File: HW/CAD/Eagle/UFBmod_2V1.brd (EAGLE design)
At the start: 98.4 x 89.5 mm, 195 parts, among them T0551 MMBT2222, U0501 MIDAS_MCCOG21605B6W-FPTLWI, U0601 MAX5217, U0701 AT86RF215-ZU, U0711 ASVTX-13-D-26.000MHZ-I05-T, U0811 PE4259, U0821 RFX1010, U0881 B39871B3440U410, U0911 FT232HL, U1101 TPS53353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

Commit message: HW - Eagle - V2.1 update to current FPGA implementation
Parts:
- R0971, R0972: value 1kR -> 560R
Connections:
- removed net FPGA_FT_RXD: JB2.83, R0962.2
- removed net FPGA_FT_TXD: JB2.81, R0961.2
- removed net UART0_RXD: JB1.91
- removed net UART0_TXD: JB1.86
- new net FPGA_UART0_RXD: JB1.91, R0961.2
- new net FPGA_UART0_TXD: JB1.86, R0962.2
- net FT_RXLED_D: now also D0971.C; no longer D0971.A
- net FT_TXLED_D: now also D0972.C; no longer D0972.A
- net FT_VCCD: now also D0971.A, D0972.A
- net GND: no longer D0971.C, D0972.C
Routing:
- net FPGA_FT_RXD: track 2.85 -> 0.00 mm
- net FPGA_UART0_TXD: track 0.00 -> 2.84 mm
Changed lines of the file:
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@@
 <attribute name="VALUE" x="68.2625" y="67.6275" size="0.6096" layer="27" font="vector" ratio="10" rot="R270"/>
 </element>
-<element name="R0971" library="df4iah_rcl" package="R0402" value="1kR" x="59.69" y="36.83" smashed="yes" rot="MR270">
+<element name="R0971" library="df4iah_rcl" package="R0402" value="560R" x="59.69" y="36.83" smashed="yes" rot="MR270">
 <attribute name="NAME" x="60.6425" y="35.2425" size="0.6096" layer="26" font="vector" ratio="10" rot="MR90"/>
 <attribute name="VALUE" x="61.2775" y="38.4175" size="0.6096" layer="28" font="vector" ratio="10" rot="MR270"/>
 </element>
-<element name="R0972" library="df4iah_rcl" package="R0402" value="1kR" x="58.42" y="36.83" smashed="yes" rot="MR270">
+<element name="R0972" library="df4iah_rcl" package="R0402" value="560R" x="58.42" y="36.83" smashed="yes" rot="MR270">
 <attribute name="NAME" x="56.8325" y="35.2425" size="0.6096" layer="26" font="vector" ratio="10" rot="MR90"/>
 <attribute name="VALUE" x="60.0075" y="38.4175" size="0.6096" layer="28" font="vector" ratio="10" rot="MR270"/>
@@
 <contactref element="C0921" pad="1"/>
 <contactref element="C0922" pad="1"/>
-<contactref element="D0971" pad="C"/>
-<contactref element="D0972" pad="C"/>
 <contactref element="X1331" pad="1"/>
 <contactref element="X1331" pad="3"/>
@@
 <wire x1="74.93" y1="21.17" x2="77.88" y2="27.96" width="0" layer="19" extent="16-16"/>
 <wire x1="54.61" y1="82.55" x2="54.545" y2="74.945" width="0" layer="19" extent="1-1"/>
-<wire x1="45.72" y1="87.41" x2="49.2125" y2="84.44" width="0" layer="19" extent="1-1"/>
-<wire x1="43.18" y1="87.41" x2="45.72" y2="87.41" width="0" layer="19" extent="1-1"/>
 <wire x1="74.93" y1="12.05" x2="74.93" y2="21.17" width="0" layer="19" extent="16-16"/>
 <wire x1="22.5425" y1="47.3075" x2="33.03" y2="46.21" width="0" layer="19" extent="1-1"/>
@@
 <wire x1="60.0075" y1="48.5425" x2="60.0075" y2="41.91" width="0.1524" layer="16"/>
 <wire x1="60.0075" y1="41.91" x2="60.325" y2="41.5925" width="0.1524" layer="16"/>
+<contactref element="D0971" pad="A"/>
+<contactref element="D0972" pad="A"/>
+<wire x1="43.18" y1="85.31" x2="45.72" y2="85.31" width="0" layer="19" extent="1-1"/>
+<wire x1="59.85" y1="48.7" x2="45.72" y2="85.31" width="0" layer="19" extent="1-16"/>
 </signal>
 <signal name="FT_RESET">
@@
 <wire x1="62.865" y1="47.625" x2="64.12" y2="47.625" width="0.1524" layer="16"/>
 </signal>
-<signal name="FPGA_FT_TXD">
-<contactref element="R0961" pad="2"/>
-<contactref element="JB2" pad="81"/>
-<wire x1="65.42" y1="47.625" x2="63.63" y2="62.81" width="0" layer="19" extent="1-16"/>
-</signal>
 <signal name="FT_RXD">
 <contactref element="U0911" pad="14"/>
@@
 <wire x1="62.5475" y1="45.72" x2="64.77" y2="66.69" width="0" layer="19" extent="1-16"/>
 </signal>
-<signal name="FPGA_FT_RXD">
-<contactref element="R0962" pad="2"/>
-<contactref element="JB2" pad="83"/>
-<wire x1="64.13" y1="62.81" x2="64.135" y2="62.815" width="0.1524" layer="1"/>
-<wire x1="64.135" y1="62.815" x2="64.135" y2="63.8175" width="0.1524" layer="1"/>
-<wire x1="64.135" y1="63.8175" x2="63.5" y2="64.4525" width="0.1524" layer="1"/>
-<wire x1="63.5" y1="64.4525" x2="63.5" y2="65.39" width="0.1524" layer="1"/>
-</signal>
 <signal name="FPGA_FT_RTS">
 <contactref element="R0963" pad="2"/>
@@
 <signal name="FT_TXLED_D">
 <contactref element="R0972" pad="2"/>
-<contactref element="D0972" pad="A"/>
-<wire x1="58.42" y1="36.18" x2="45.72" y2="85.31" width="0" layer="19" extent="1-16"/>
+<contactref element="D0972" pad="C"/>
+<wire x1="58.42" y1="36.18" x2="45.72" y2="87.41" width="0" layer="19" extent="1-16"/>
 </signal>
 <signal name="FT_RXLED_D">
 <contactref element="R0971" pad="2"/>
-<contactref element="D0971" pad="A"/>
-<wire x1="59.69" y1="36.18" x2="43.18" y2="85.31" width="0" layer="19" extent="1-16"/>
+<contactref element="D0971" pad="C"/>
+<wire x1="59.69" y1="36.18" x2="43.18" y2="87.41" width="0" layer="19" extent="1-16"/>
 </signal>
 <signal name="B2W_51">
@@
 <wire x1="4.43" y1="53.34" x2="56.13" y2="59.11" width="0" layer="19" extent="1-1"/>
 </signal>
-<signal name="UART0_TXD">
+<signal name="FPGA_UART0_TXD">
 <contactref element="JB1" pad="86"/>
+<contactref element="R0962" pad="2"/>
+<wire x1="64.135" y1="62.815" x2="64.135" y2="63.8175" width="0.1524" layer="1"/>
+<wire x1="64.135" y1="63.8175" x2="63.5" y2="64.4525" width="0.1524" layer="1"/>
+<wire x1="63.5" y1="64.4525" x2="63.5" y2="65.39" width="0.1524" layer="1"/>
+<wire x1="64.63" y1="27.11" x2="64.135" y2="62.815" width="0" layer="19" extent="1-1"/>
 </signal>
-<signal name="UART0_RXD">
+<signal name="FPGA_UART0_RXD">
 <contactref element="JB1" pad="91"/>
+<contactref element="R0961" pad="2"/>
+<wire x1="66.13" y1="30.81" x2="65.42" y2="47.625" width="0" layer="19" extent="1-16"/>
 </signal>
 </signals>

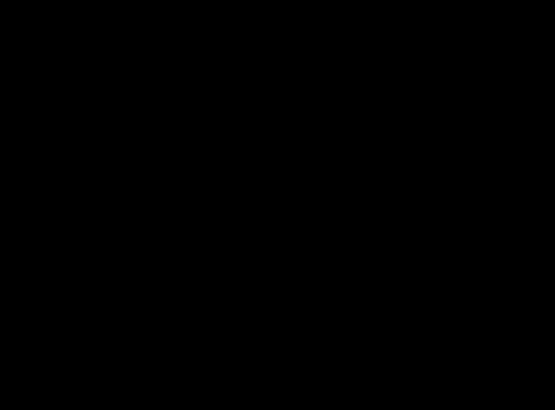
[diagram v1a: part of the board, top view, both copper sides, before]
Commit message: HW - Eagle - V2.1 some signals fixed
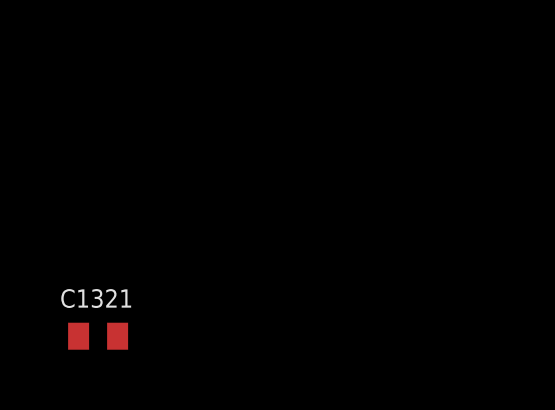
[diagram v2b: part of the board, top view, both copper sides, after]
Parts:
- added C1321: 100nF, df4iah_rcl:C0402
- R1321: value 100R -> 1kR
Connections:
- net FPGA_RESET: now also C1321.2; no longer JB3.41
- net GND: now also C1321.1
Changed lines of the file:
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@@
 </element>
 <element name="S1321" library="df4iah_switch" package="KSR223G_SMD_1POL" value="KSR223G_SMD_1POL" x="36.83" y="73.66" rot="R90"/>
-<element name="R1321" library="df4iah_rcl" package="R0402" value="100R" x="36.83" y="67.31" rot="R90"/>
+<element name="R1321" library="df4iah_rcl" package="R0402" value="1kR" x="36.83" y="67.31" rot="R90"/>
 <element name="R0711" library="df4iah_rcl" package="R0402" value="100R" x="5.08" y="53.34"/>
+<element name="C1321" library="df4iah_rcl" package="C0402" value="100nF" x="-21.59" y="-26.67"/>
 </elements>
 <signals>
@@
 <wire x1="53.6575" y1="44.1325" x2="53.975" y2="44.45" width="0.1524" layer="16"/>
 <via x="53.975" y="44.45" extent="1-16" drill="0.3"/>
+<contactref element="C1321" pad="1"/>
 <wire x1="92.71" y1="74.77" x2="93.345" y2="84.455" width="0" layer="19" extent="1-1"/>
 <wire x1="83.82" y1="76.2" x2="92.71" y2="74.77" width="0" layer="19" extent="1-1"/>
@@
 <wire x1="94.8563" y1="53.1241" x2="94.8563" y2="50.8" width="0" layer="19" extent="16-16"/>
 <wire x1="93.345" y1="5.08" x2="74.93" y2="12.05" width="0" layer="19" extent="16-16"/>
+<wire x1="-22.24" y1="-26.67" x2="5.08" y2="5.08" width="0" layer="19" extent="1-1"/>
 </signal>
 <signal name="+3V3">
@@
 </signal>
 <signal name="FPGA_RESET">
-<contactref element="JB3" pad="41"/>
 <contactref element="JB3" pad="43"/>
 <contactref element="R1321" pad="1"/>
-<wire x1="33.03" y1="48.21" x2="33.03" y2="47.71" width="0" layer="19" extent="1-1"/>
-<wire x1="36.83" y1="66.66" x2="33.03" y2="47.71" width="0" layer="19" extent="1-1"/>
+<contactref element="C1321" pad="2"/>
+<wire x1="33.03" y1="48.21" x2="36.83" y2="66.66" width="0" layer="19" extent="1-1"/>
+<wire x1="-20.94" y1="-26.67" x2="33.03" y2="48.21" width="0" layer="19" extent="1-1"/>
 </signal>
 <signal name="FPGA_RESET_R">

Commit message: HW - Eagle - V2.1 UART part fixed
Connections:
- net FPGA_FT_CTS renamed FPGA_FT_CTSN
- net FPGA_FT_DCD renamed FPGA_FT_DCDN
- net FPGA_FT_DSR renamed FPGA_FT_DSRN
- net FPGA_FT_DTR renamed FPGA_FT_DTRN
- net FPGA_FT_RESET renamed FPGA_FT_RESETN
- net FPGA_FT_RI renamed FPGA_FT_RIN
- net FPGA_FT_RTS renamed FPGA_FT_RTSN
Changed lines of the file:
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@@
 <wire x1="55.23" y1="37.465" x2="53.355" y2="37.465" width="0.1524" layer="16"/>
 </signal>
-<signal name="FPGA_FT_RESET">
+<signal name="FPGA_FT_RESETN">
 <contactref element="R0912" pad="1"/>
 <contactref element="JB2" pad="77"/>
@@
 <wire x1="62.5475" y1="45.72" x2="64.77" y2="66.69" width="0" layer="19" extent="1-16"/>
 </signal>
-<signal name="FPGA_FT_RTS">
+<signal name="FPGA_FT_RTSN">
 <contactref element="R0963" pad="2"/>
 <contactref element="JB2" pad="85"/>
 <wire x1="65.42" y1="46.355" x2="64.63" y2="62.81" width="0" layer="19" extent="1-16"/>
 </signal>
-<signal name="FPGA_FT_CTS">
+<signal name="FPGA_FT_CTSN">
 <contactref element="R0964" pad="2"/>
 <contactref element="JB2" pad="87"/>
@@
 <wire x1="62.5475" y1="43.815" x2="69.85" y2="66.69" width="0" layer="19" extent="1-16"/>
 </signal>
-<signal name="FPGA_FT_DSR">
+<signal name="FPGA_FT_DSRN">
 <contactref element="R0966" pad="2"/>
 <contactref element="JB2" pad="93"/>
@@
 <wire x1="66.04" y1="64.77" x2="66.04" y2="65.39" width="0.1524" layer="1"/>
 </signal>
-<signal name="FPGA_FT_DTR">
+<signal name="FPGA_FT_DTRN">
 <contactref element="R0965" pad="2"/>
 <contactref element="JB2" pad="91"/>
 <wire x1="65.42" y1="45.085" x2="66.13" y2="62.81" width="0" layer="19" extent="1-16"/>
 </signal>
-<signal name="FPGA_FT_DCD">
+<signal name="FPGA_FT_DCDN">
 <contactref element="R0967" pad="2"/>
 <contactref element="JB2" pad="95"/>
@@
 <wire x1="67.945" y1="64.77" x2="67.945" y2="65.39" width="0.1524" layer="1"/>
 </signal>
-<signal name="FPGA_FT_RI">
+<signal name="FPGA_FT_RIN">
 <contactref element="R0968" pad="2"/>
 <contactref element="JB2" pad="97"/>

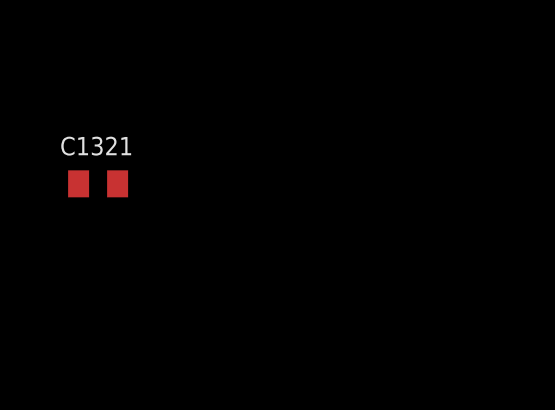
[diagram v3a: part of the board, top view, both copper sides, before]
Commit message: HW - Eagle - V2.1 clock loop-back from FPGA out to extPLL in added
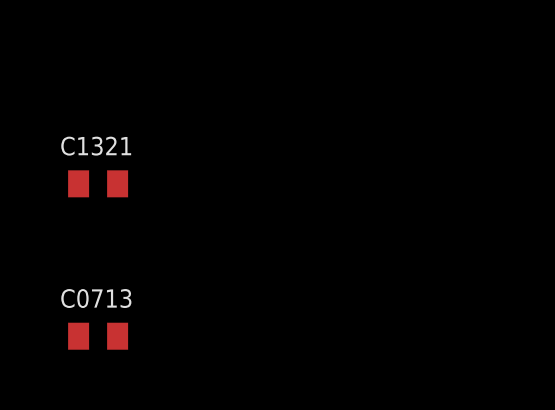
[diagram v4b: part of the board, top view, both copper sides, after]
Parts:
- added C0713: 1nF, df4iah_rcl:C0402
- R0711: value 100R -> 33R
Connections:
- new net CLKIN2_N: JB3.31, JB3.39
- new net CLKIN2_P: JB3.33, JB3.37
- net GND: now also C0713.1
- net TRX_CLK_26MHZ: now also C0713.2
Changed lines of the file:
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@@
 <element name="S1321" library="df4iah_switch" package="KSR223G_SMD_1POL" value="KSR223G_SMD_1POL" x="36.83" y="73.66" rot="R90"/>
 <element name="R1321" library="df4iah_rcl" package="R0402" value="1kR" x="36.83" y="67.31" rot="R90"/>
-<element name="R0711" library="df4iah_rcl" package="R0402" value="100R" x="5.08" y="53.34"/>
+<element name="R0711" library="df4iah_rcl" package="R0402" value="33R" x="5.08" y="53.34"/>
 <element name="C1321" library="df4iah_rcl" package="C0402" value="100nF" x="-21.59" y="-26.67"/>
+<element name="C0713" library="df4iah_rcl" package="C0402" value="1nF" x="-21.59" y="-31.75"/>
 </elements>
 <signals>
@@
 <via x="53.975" y="44.45" extent="1-16" drill="0.3"/>
 <contactref element="C1321" pad="1"/>
+<contactref element="C0713" pad="1"/>
 <wire x1="92.71" y1="74.77" x2="93.345" y2="84.455" width="0" layer="19" extent="1-1"/>
 <wire x1="83.82" y1="76.2" x2="92.71" y2="74.77" width="0" layer="19" extent="1-1"/>
@@
 <wire x1="93.345" y1="5.08" x2="74.93" y2="12.05" width="0" layer="19" extent="16-16"/>
 <wire x1="-22.24" y1="-26.67" x2="5.08" y2="5.08" width="0" layer="19" extent="1-1"/>
+<wire x1="-22.24" y1="-31.75" x2="-22.24" y2="-26.67" width="0" layer="19" extent="1-1"/>
 </signal>
 <signal name="+3V3">
@@
 <contactref element="R0711" pad="1"/>
 <contactref element="JB2" pad="52"/>
+<contactref element="C0713" pad="2"/>
 <wire x1="4.43" y1="53.34" x2="56.13" y2="59.11" width="0" layer="19" extent="1-1"/>
+<wire x1="-20.94" y1="-31.75" x2="4.43" y2="53.34" width="0" layer="19" extent="1-1"/>
 </signal>
 <signal name="FPGA_UART0_TXD">
@@
 <wire x1="66.13" y1="30.81" x2="65.42" y2="47.625" width="0" layer="19" extent="1-16"/>
 </signal>
+<signal name="CLKIN2_N">
+<contactref element="JB3" pad="31"/>
+<contactref element="JB3" pad="39"/>
+<wire x1="33.03" y1="45.21" x2="33.03" y2="47.21" width="0" layer="19" extent="1-1"/>
+</signal>
+<signal name="CLKIN2_P">
+<contactref element="JB3" pad="33"/>
+<contactref element="JB3" pad="37"/>
+<wire x1="33.03" y1="45.71" x2="33.03" y2="46.71" width="0" layer="19" extent="1-1"/>
+</signal>
 </signals>

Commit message: HW - Eagle - V2.1 LVDS dummy output TXD[1] added
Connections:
- new net TRX_TXD_VOID_N: JB3.49
- new net TRX_TXD_VOID_P: JB3.47
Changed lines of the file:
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@@
 <wire x1="33.03" y1="45.71" x2="33.03" y2="46.71" width="0" layer="19" extent="1-1"/>
+</signal>
+<signal name="TRX_TXD_VOID_N">
+<contactref element="JB3" pad="49"/>
+</signal>
+<signal name="TRX_TXD_VOID_P">
+<contactref element="JB3" pad="47"/>
 </signal>
 </signals>

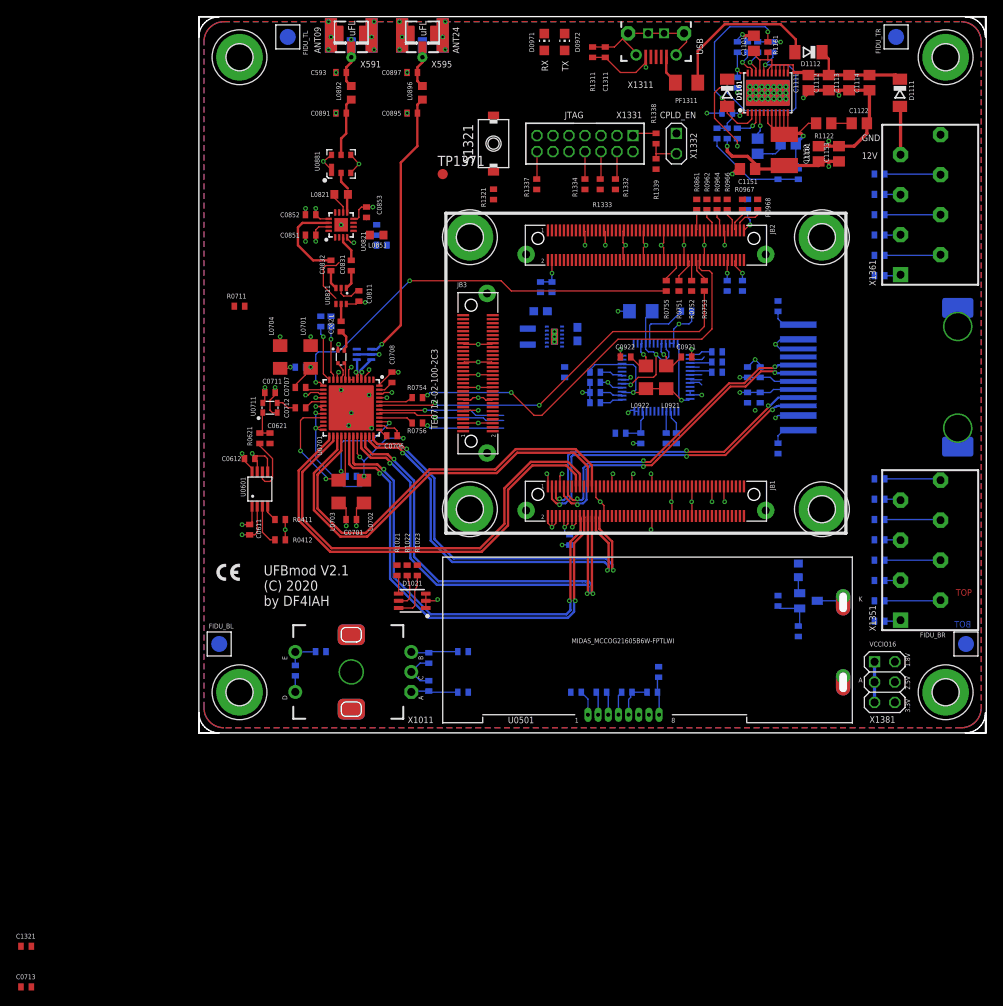
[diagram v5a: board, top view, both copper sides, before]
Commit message: HW_2V0 - CAD/Eagle - TRX frontend routed
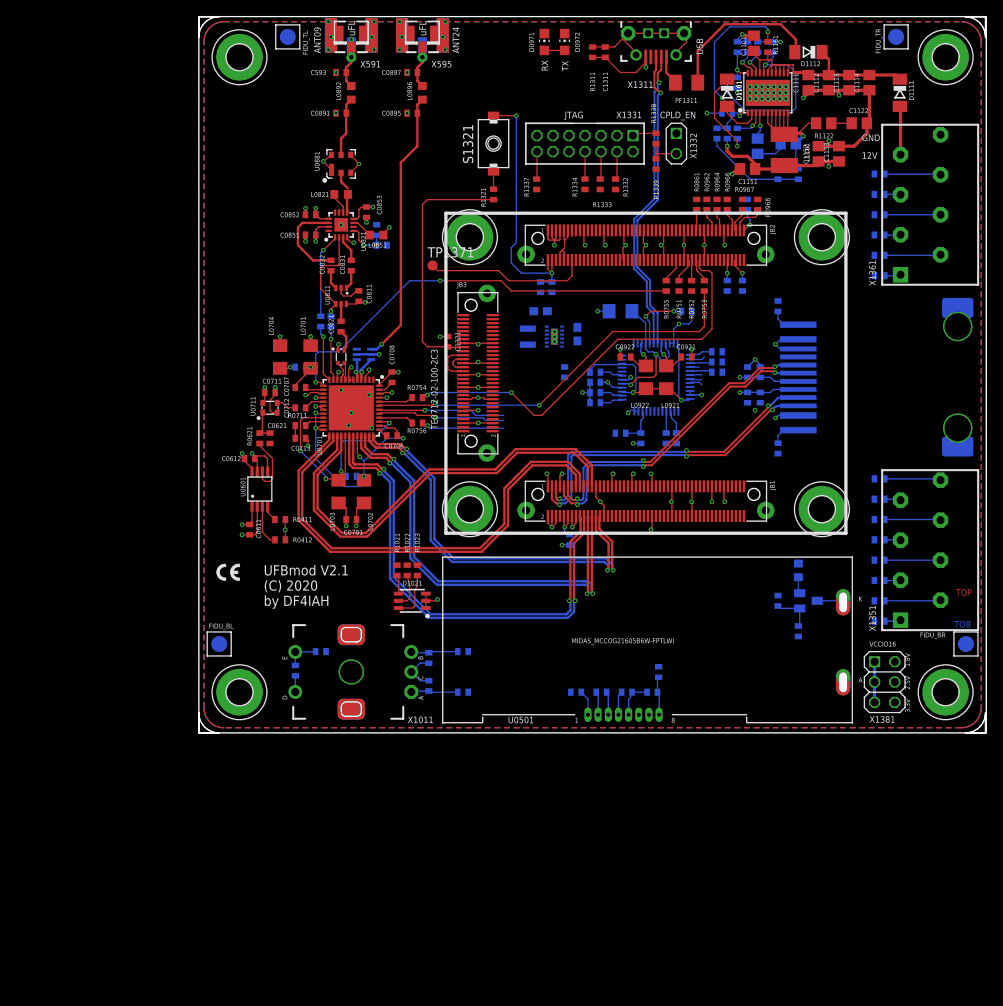
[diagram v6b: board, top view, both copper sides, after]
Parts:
- moved C1321 92.1 mm to (31.1, 48.9), turned to 270 degrees
- moved C0713 76.7 mm to (12.7, 36.8), turned to 180 degrees
- moved R0711 16.8 mm to (12.7, 38.4)
- moved TP1371 11.5 mm to (29.2, 58.4)
- moved L0911 2.54 mm to (52.7, 52.7)
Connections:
- net USB_D_M renamed USB_D_N
- net BOARD_LCD_RESETN: now also JB1.98
- net DDR3_INIT_CALIB_COMPLETE: now also JB2.14
- net FPGA_LCD_BL_PWM: now also JB1.96
- net FPGA_LED_RGB_BLUE: now also JB1.100
- net FPGA_LED_RGB_GREEN: now also JB1.94
- net FPGA_LED_RGB_RED: now also JB1.92
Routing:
- net USB_D_N: track 0.00 -> 38.6 mm, vias 0 -> 1
- net USB_D_P: track 0.00 -> 38.5 mm, vias 0 -> 1
- net FPGA_RESET: track 0.00 -> 31.7 mm
- net VCCIO13: track 4.17 -> 33.2 mm, vias 1 -> 2
- net DDR3_INIT_CALIB_COMPLETE: track 0.00 -> 20.5 mm
- net RFX_TXEN: track 0.00 -> 13.0 mm, vias 0 -> 1
- net RFX_RXEN: track 0.00 -> 10.6 mm, vias 0 -> 1
- net +3V3: track 74.7 -> 83.4 mm, vias 17 -> 20
- net TRX_FEA09: track 13.5 -> 6.79 mm
- net U3V3: track 0.00 -> 6.68 mm
- net CLKIN2_N: track 0.00 -> 5.50 mm
- net RFX_DET: track 0.00 -> 5.44 mm, vias 0 -> 1
- net CLKIN2_P: track 0.00 -> 3.16 mm
- net RFX_VDD3: track 0.00 -> 2.67 mm
- net FT_VCCD: track 26.5 -> 29.1 mm
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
